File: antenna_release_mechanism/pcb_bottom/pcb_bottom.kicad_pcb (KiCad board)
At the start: 2 copper layers, 96 x 79 mm, 9 parts

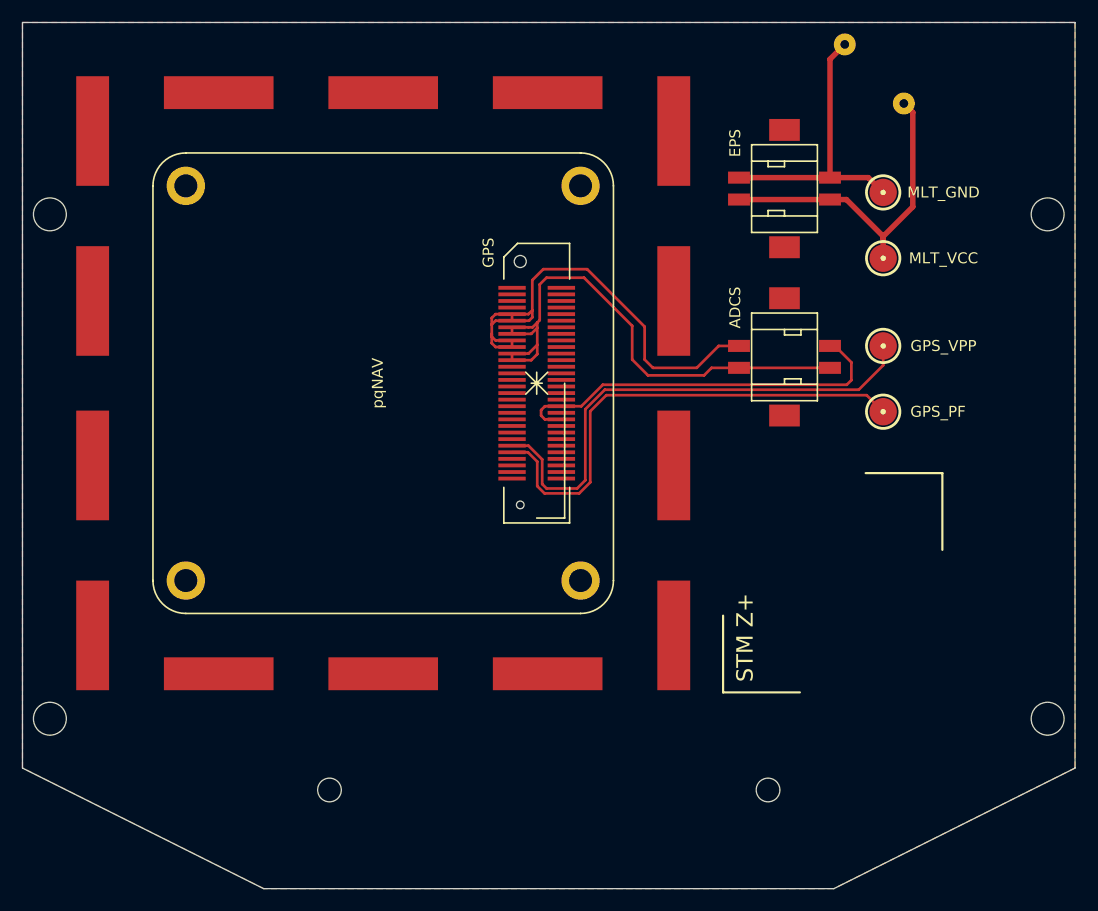
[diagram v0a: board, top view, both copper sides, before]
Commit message: ANT bottom antenna for GPS housing and melt line.
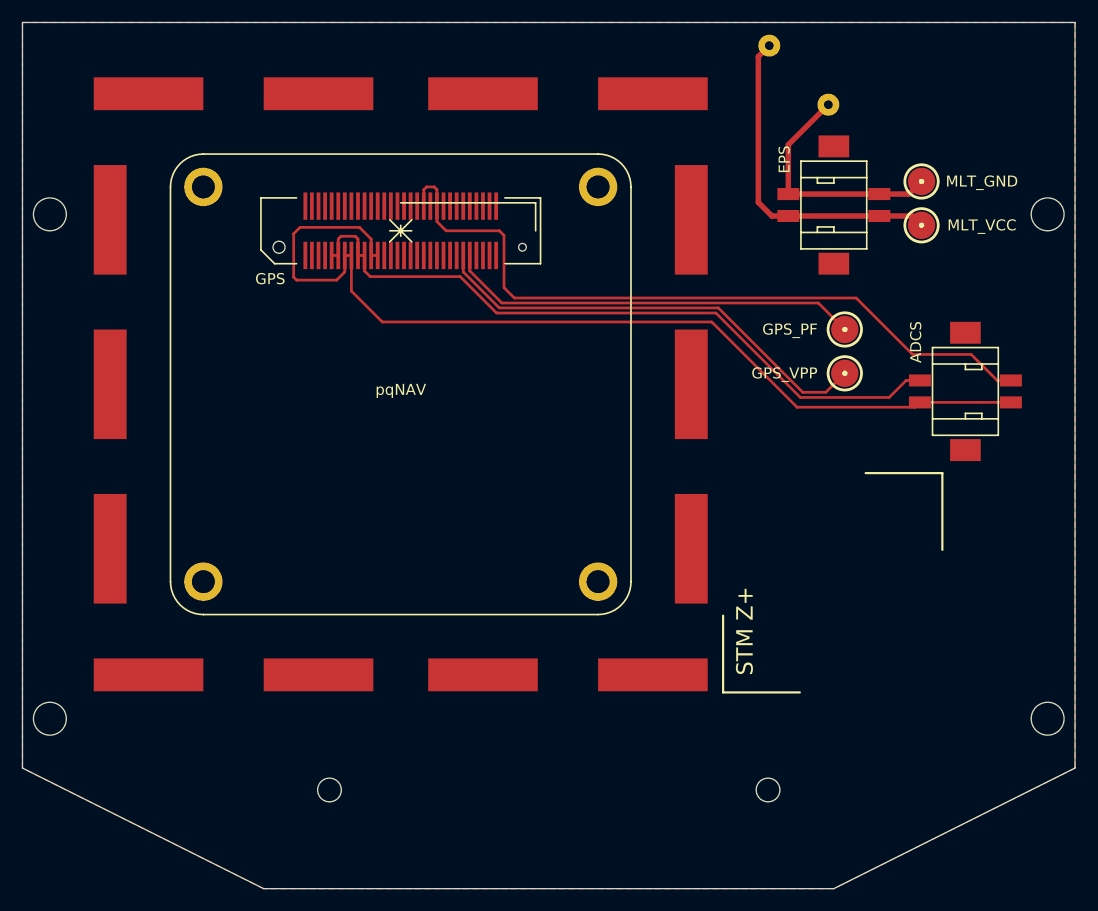
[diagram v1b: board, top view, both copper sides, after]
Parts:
- added G***: LOGO, w_logo:Logo_silk_OSHW_12x13mm, B.Cu at (174.0, 77.0)
- added G***: LOGO, libs:upsat-logo, B.Cu at (108.5, 75.0)
- moved GPS 18.6 mm to (126.0, 86.5), turned to 0 degrees
- moved ADCS 16.8 mm to (177.5, 101.2)
- moved GPS_PF 8.28 mm to (166.5, 95.5)
- moved R1 6.89 mm to (162.3, 72.3), turned to 315 degrees
- moved EPS 4.74 mm to (165.5, 84.2)
- moved MLT_VCC 4.61 mm to (173.5, 86.0)
- moved GPS_VPP 4.30 mm to (166.5, 99.5)
- moved MLT_GND 3.64 mm to (173.5, 82.0)
- moved pqNAV 1.60 mm to (126.0, 100.5), turned to 0 degrees
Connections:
- pqNAV pad 1: (no net) -> /GPS_GND
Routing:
- net /GPS_GND: track 50.3 -> 89.0 mm
- net /GPS_TXD: track 36.1 -> 67.0 mm
- net /GPS_VDD: track 44.7 -> 63.7 mm
- net /GPS_PF: track 44.8 -> 37.8 mm
- net /GPS_VPP: track 47.0 -> 41.6 mm
- net /MELT_GND: track 26.4 -> 22.3 mm
- net /MELT_VCC: track 30.3 -> 30.9 mm
